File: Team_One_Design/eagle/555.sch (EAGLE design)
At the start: 9 parts, among them P1 1k, P2 1k

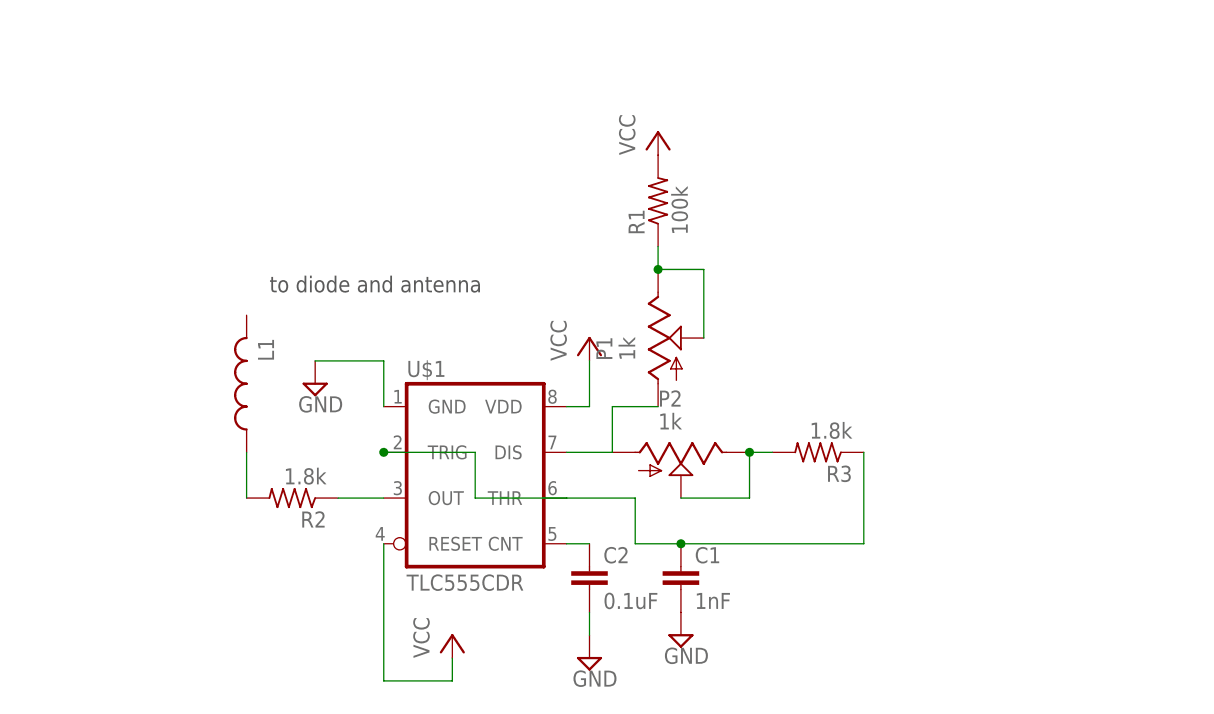
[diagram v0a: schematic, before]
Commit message: added datasheet for new RF diode, updated schem and layout for 555 circuit.
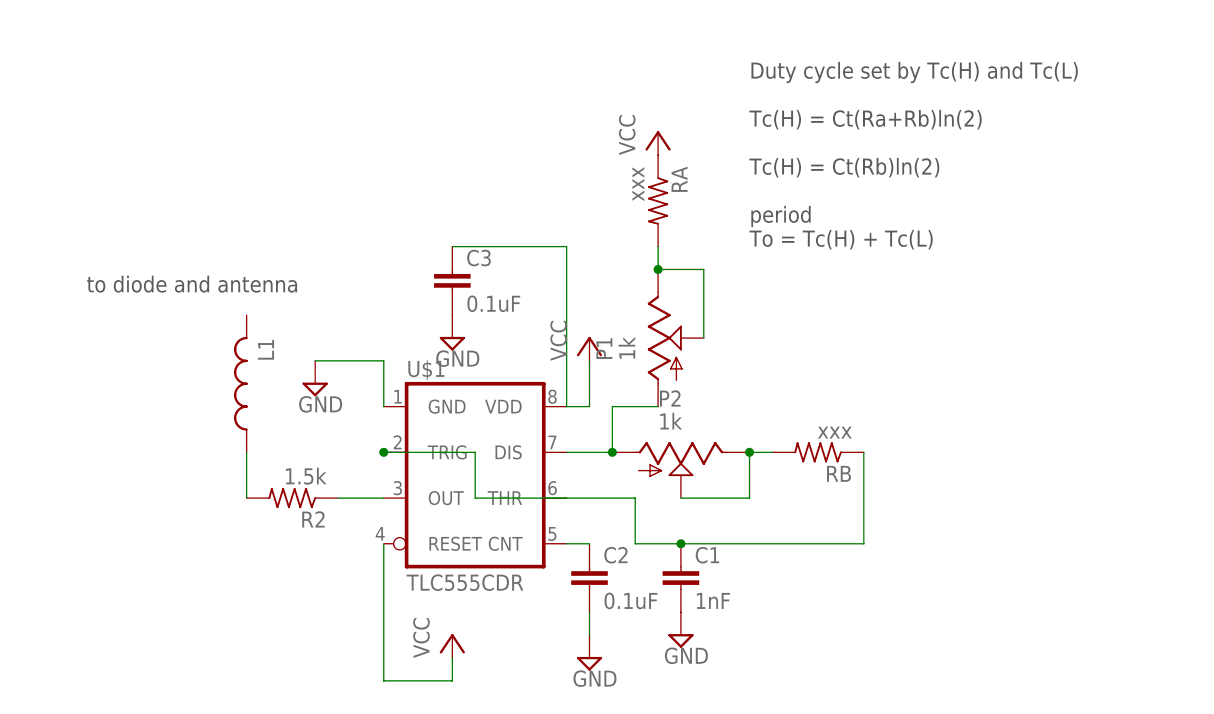
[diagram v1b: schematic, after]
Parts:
- removed R1: 100k, resistor:R-US_0204/7
- added C3: 0.1uF, resistor:C-EU050-024X044
- added RA: xxx, resistor:R-US_R0805
- C1, C2: device resistor:C-EUC0805 -> resistor:C-EU050-024X044
- R2: value 1.8k -> 1.5k
- RB: value 1.8k -> xxx
- renumbered R3 to RB
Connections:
- net GND: now also C3.2
- net N$6: now also RA.2; no longer R1.1
- net VCC: now also C3.1, RA.1; no longer R1.2
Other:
- note added: "Duty cycle set by Tc(H) and Tc(L) Tc(H) = Ct(Ra+Rb)ln(2) Tc(H) = Ct(Rb)ln(2) period To = Tc(H) + Tc(L)"
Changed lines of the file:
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@@
 <part name="P+2" library="supply1" deviceset="VCC" device=""/>
 <part name="P+3" library="supply1" deviceset="VCC" device=""/>
-<part name="R1" library="resistor" deviceset="R-US_" device="0204/7" value="100k"/>
 <part name="SUPPLY3" library="supply2" deviceset="GND" device=""/>
-<part name="C1" library="resistor" deviceset="C-EU" device="C0805" value="1nF"/>
-<part name="C2" library="resistor" deviceset="C-EU" device="C0805" value="0.1uF"/>
+<part name="C1" library="resistor" deviceset="C-EU" device="050-024X044" value="1nF"/>
+<part name="C2" library="resistor" deviceset="C-EU" device="050-024X044" value="0.1uF"/>
 <part name="SUPPLY4" library="supply2" deviceset="GND" device=""/>
 <part name="P1" library="potentiometer" deviceset="TRIM_US-" device="3223J" value="1k"/>
 <part name="L1" library="resistor" deviceset="L-US" device="L2012C"/>
 <part name="U$1" library="ece510_library" deviceset="TLC555CDR" device=""/>
-<part name="R3" library="resistor" deviceset="R-US_" device="R0805" value="1.8k"/>
+<part name="RB" library="resistor" deviceset="R-US_" device="R0805" value="xxx"/>
 <part name="P2" library="potentiometer" deviceset="TRIM_US-" device="3223J" value="1k"/>
-<part name="R2" library="resistor" deviceset="R-US_" device="R0805" value="1.8k"/>
+<part name="R2" library="resistor" deviceset="R-US_" device="R0805" value="1.5k"/>
+<part name="C3" library="resistor" deviceset="C-EU" device="050-024X044" value="0.1uF"/>
+<part name="SUPPLY2" library="supply2" deviceset="GND" device=""/>
+<part name="RA" library="resistor" deviceset="R-US_" device="R0805" value="xxx"/>
 </parts>
 <sheets>
 <sheet>
 <plain>
-<text x="55.88" y="73.66" size="1.778" layer="97">to diode and antenna</text>
+<text x="35.56" y="73.66" size="1.778" layer="97">to diode and antenna</text>
+<text x="109.22" y="78.74" size="1.778" layer="97">Duty cycle set by Tc(H) and Tc(L)
+Tc(H) = Ct(Ra+Rb)ln(2)
+Tc(H) = Ct(Rb)ln(2)
+period
+To = Tc(H) + Tc(L)</text>
 </plain>
 <instances>
@@
 <instance part="P+2" gate="VCC" x="99.06" y="91.44"/>
 <instance part="P+3" gate="VCC" x="76.2" y="35.56"/>
-<instance part="R1" gate="G$1" x="99.06" y="83.82" rot="R90"/>
 <instance part="SUPPLY3" gate="GND" x="60.96" y="63.5"/>
 <instance part="C1" gate="G$1" x="101.6" y="43.18"/>
@@
 <instance part="L1" gate="G$1" x="53.34" y="63.5" rot="R180"/>
 <instance part="U$1" gate="G$1" x="78.74" y="53.34"/>
-<instance part="R3" gate="G$1" x="116.84" y="55.88" rot="R180"/>
+<instance part="RB" gate="G$1" x="116.84" y="55.88" rot="R180"/>
 <instance part="P2" gate="G$1" x="101.6" y="55.88" rot="R270"/>
 <instance part="R2" gate="G$1" x="58.42" y="50.8" rot="R180"/>
+<instance part="C3" gate="G$1" x="76.2" y="76.2"/>
+<instance part="SUPPLY2" gate="GND" x="76.2" y="68.58"/>
+<instance part="RA" gate="G$1" x="99.06" y="83.82" rot="R270"/>
 </instances>
 <busses>
@@
 <pinref part="C1" gate="G$1" pin="2"/>
 <pinref part="SUPPLY1" gate="GND" pin="GND"/>
+</segment>
+<segment>
+<pinref part="C3" gate="G$1" pin="2"/>
+<pinref part="SUPPLY2" gate="GND" pin="GND"/>
 </segment>
 </net>
@@
 <pinref part="P+1" gate="VCC" pin="VCC"/>
 <wire x1="91.44" y1="60.96" x2="91.44" y2="66.04" width="0.1524" layer="91"/>
+<wire x1="88.9" y1="60.96" x2="88.9" y2="78.74" width="0.1524" layer="91"/>
+<pinref part="C3" gate="G$1" pin="1"/>
+<wire x1="88.9" y1="78.74" x2="76.2" y2="78.74" width="0.1524" layer="91"/>
 </segment>
 <segment>
-<pinref part="R1" gate="G$1" pin="2"/>
 <pinref part="P+2" gate="VCC" pin="VCC"/>
+<pinref part="RA" gate="G$1" pin="1"/>
 </segment>
 </net>
@@
 <pinref part="C1" gate="G$1" pin="1"/>
 <wire x1="96.52" y1="45.72" x2="101.6" y2="45.72" width="0.1524" layer="91"/>
-<pinref part="R3" gate="G$1" pin="1"/>
+<pinref part="RB" gate="G$1" pin="1"/>
 <wire x1="121.92" y1="55.88" x2="121.92" y2="45.72" width="0.1524" layer="91"/>
 <wire x1="121.92" y1="45.72" x2="101.6" y2="45.72" width="0.1524" layer="91"/>
@@
 <pinref part="P1" gate="G$1" pin="A"/>
 <wire x1="93.98" y1="60.96" x2="99.06" y2="60.96" width="0.1524" layer="91"/>
+<junction x="93.98" y="55.88"/>
 </segment>
 </net>
 <net name="N$5" class="0">
 <segment>
-<pinref part="R3" gate="G$1" pin="2"/>
+<pinref part="RB" gate="G$1" pin="2"/>
 <pinref part="P2" gate="G$1" pin="E"/>
 <wire x1="109.22" y1="55.88" x2="111.76" y2="55.88" width="0.1524" layer="91"/>
@@
 <segment>
 <pinref part="P1" gate="G$1" pin="E"/>
-<pinref part="R1" gate="G$1" pin="1"/>
 <wire x1="99.06" y1="78.74" x2="99.06" y2="76.2" width="0.1524" layer="91"/>
 <wire x1="99.06" y1="76.2" x2="104.14" y2="76.2" width="0.1524" layer="91"/>
 <junction x="99.06" y="76.2"/>
+<pinref part="RA" gate="G$1" pin="2"/>
 </segment>
 </net>
@@
 </schematic>
 </drawing>
+<compatibility>
+<note version="6.3" minversion="6.2.2" severity="warning">
+Since Version 6.2.2 text objects can contain more than one line,
+which will not be processed correctly with this version.
+</note>
+</compatibility>
 </eagle>

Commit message: updated schematic and layout of 555 timer board
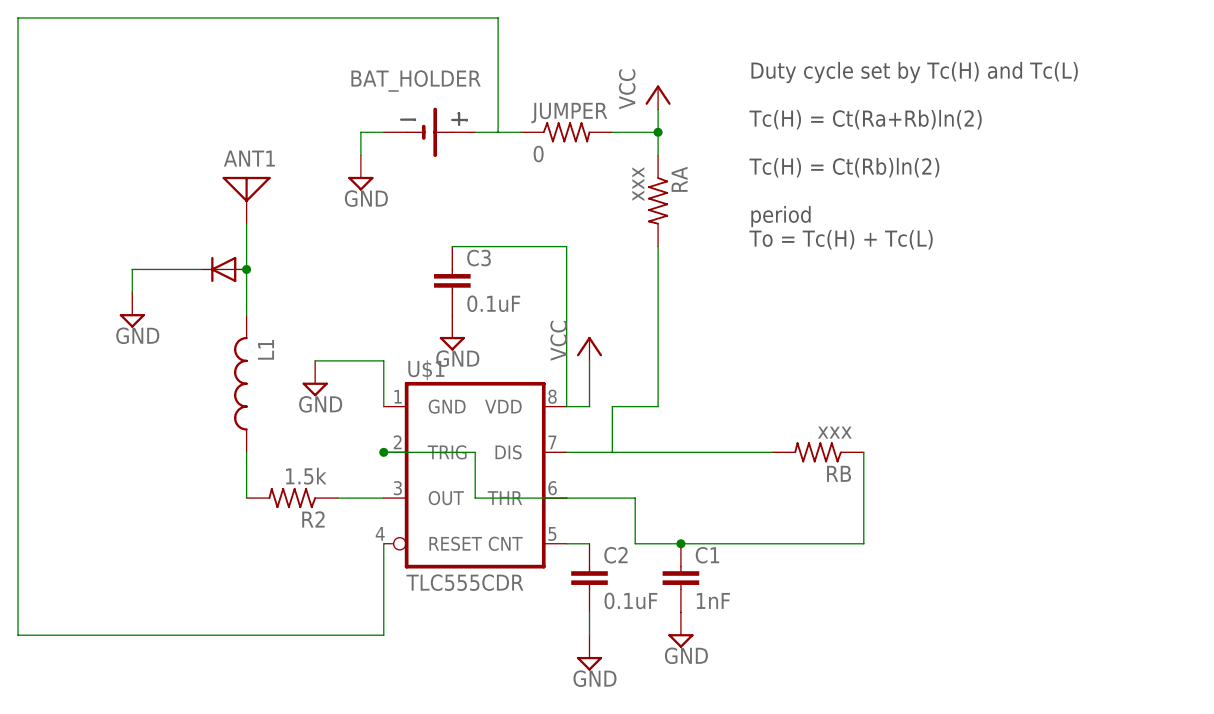
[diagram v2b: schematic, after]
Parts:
- removed P1, P2: 1k, potentiometer:TRIM_US-3223J
- added ANT1: (no value), discrete:ANTENNA
- added JUMPER: 0, resistor:R-US_R0805
- added U$2: BAT_HOLDER, ece510_library:BAT_HOLDER
- added U$3: BAT-15-03W, ece510_library:BAT-15-03W
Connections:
- removed net N$5: P2.E, P2.S, RB.2
- removed net N$6: P1.E, RA.2
- new net N$9: ANT1.1, L1.2, U$3.A
- net GND: now also U$2.-, U$3.C
- net N$1: now also RA.2, RB.2; no longer P1.A, P2.A
- net N$3: now also JUMPER.1, U$1.RESET, U$2.+; no longer P1.S
- net VCC: now also JUMPER.2; no longer U$1.RESET
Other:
- note removed: "to diode and antenna"

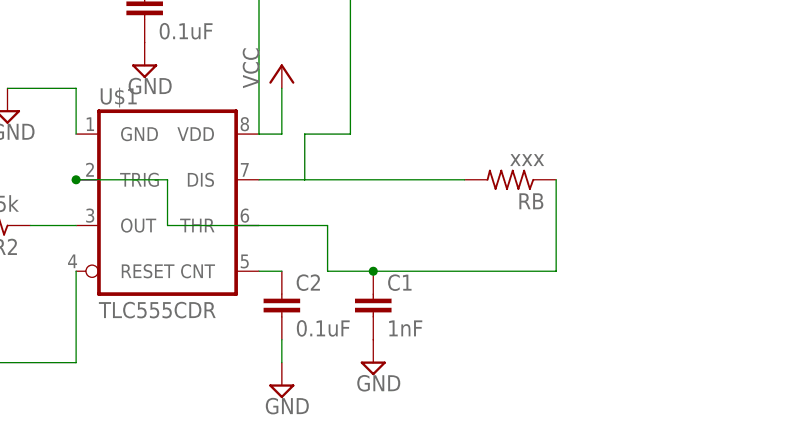
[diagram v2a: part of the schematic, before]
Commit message: added dimmesnsions to target layout
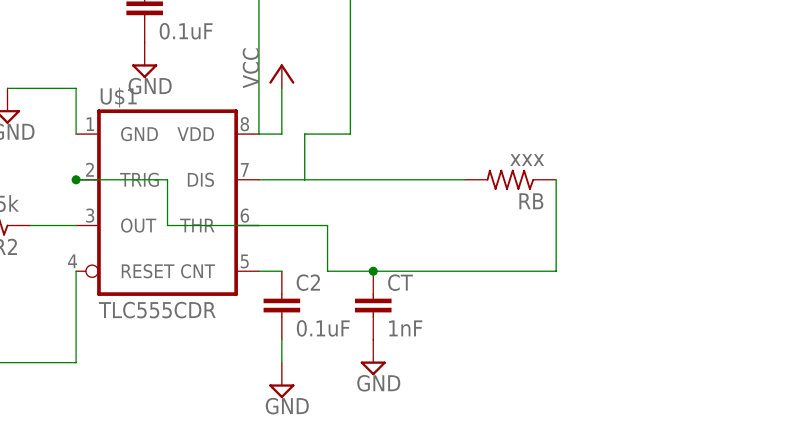
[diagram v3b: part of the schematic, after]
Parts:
- JUMPER, R2, RA, RB: device resistor:R-US_R0805 -> rcl:R-US_M1206
- renumbered C1 to CT
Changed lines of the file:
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@@
 <part name="P+1" library="supply1" deviceset="VCC" device=""/>
 <part name="SUPPLY3" library="supply2" deviceset="GND" device=""/>
-<part name="C1" library="resistor" deviceset="C-EU" device="050-024X044" value="1nF"/>
+<part name="CT" library="resistor" deviceset="C-EU" device="050-024X044" value="1nF"/>
 <part name="C2" library="resistor" deviceset="C-EU" device="050-024X044" value="0.1uF"/>
 <part name="SUPPLY4" library="supply2" deviceset="GND" device=""/>
 <part name="L1" library="resistor" deviceset="L-US" device="L2012C"/>
 <part name="U$1" library="ece510_library" deviceset="TLC555CDR" device=""/>
-<part name="RB" library="resistor" deviceset="R-US_" device="R0805" value="xxx"/>
-<part name="R2" library="resistor" deviceset="R-US_" device="R0805" value="1.5k"/>
+<part name="RB" library="rcl" deviceset="R-US_" device="M1206" value="xxx"/>
+<part name="R2" library="rcl" deviceset="R-US_" device="M1206" value="1.5k"/>
 <part name="C3" library="resistor" deviceset="C-EU" device="050-024X044" value="0.1uF"/>
 <part name="SUPPLY2" library="supply2" deviceset="GND" device=""/>
-<part name="RA" library="resistor" deviceset="R-US_" device="R0805" value="xxx"/>
+<part name="RA" library="rcl" deviceset="R-US_" device="M1206" value="xxx"/>
 <part name="U$2" library="ece510_library" deviceset="BAT_HOLDER" device=""/>
 <part name="SUPPLY5" library="supply2" deviceset="GND" device=""/>
@@
 <part name="ANT1" library="discrete" deviceset="ANTENNA" device=""/>
 <part name="U$3" library="ece510_library" deviceset="BAT-15-03W" device=""/>
-<part name="JUMPER" library="resistor" deviceset="R-US_" device="R0805" value="0"/>
+<part name="JUMPER" library="rcl" deviceset="R-US_" device="M1206" value="0"/>
 <part name="SUPPLY6" library="supply2" deviceset="GND" device=""/>
 </parts>
@@
 <instance part="P+1" gate="VCC" x="91.44" y="68.58"/>
 <instance part="SUPPLY3" gate="GND" x="60.96" y="63.5"/>
-<instance part="C1" gate="G$1" x="101.6" y="43.18"/>
+<instance part="CT" gate="G$1" x="101.6" y="43.18"/>
 <instance part="C2" gate="G$1" x="91.44" y="43.18"/>
 <instance part="SUPPLY4" gate="GND" x="91.44" y="33.02"/>
@@
 </segment>
 <segment>
-<pinref part="C1" gate="G$1" pin="2"/>
+<pinref part="CT" gate="G$1" pin="2"/>
 <pinref part="SUPPLY1" gate="GND" pin="GND"/>
 </segment>
@@
 <wire x1="88.9" y1="50.8" x2="96.52" y2="50.8" width="0.1524" layer="91"/>
 <wire x1="96.52" y1="50.8" x2="96.52" y2="45.72" width="0.1524" layer="91"/>
-<pinref part="C1" gate="G$1" pin="1"/>
+<pinref part="CT" gate="G$1" pin="1"/>
 <wire x1="96.52" y1="45.72" x2="101.6" y2="45.72" width="0.1524" layer="91"/>
 <pinref part="RB" gate="G$1" pin="1"/>
